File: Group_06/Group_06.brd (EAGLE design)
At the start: 100 x 80 mm, 18 parts, among them J1 POWER_JACKPTH_LOCK, U2 +12v

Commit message: CY8
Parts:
- added D1: BLUE, SparkFun-LED:LED-1206
- added J3: (no value), SparkFun-Connectors:1X06_LOCK
- added R11: (no value), SparkFun-Resistors:AXIAL-0.3
- added U$2: CY8CKIT-059_TARGET_3, CY8KIT-059:CY8CKIT-059_TARGET_3
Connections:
- new net GND2: U$2.52
- new net MUX_A0/2.3C: U$2.24
- new net MUX_A1/2.3C: U$2.23
- new net MUX_A2/2.3C: U$2.22
- new net MUX_OUT/2.5C: U$2.21
- new net N$2: D1.C, R11.P$2
- new net N$3: D1.A, U$2.51
- new net N$4: J3.6, U$2.37
- new net N$5: J3.5, U$2.36
- new net N$6: J3.4, U$2.35
- new net N$7: J3.3, U$2.34
- new net N$8: J3.2, U$2.33
- new net N$9: J3.1, U$2.32
- net 5V: now also U$2.26, U$2.27
- net GND: now also R11.P$1, U$2.25, U$2.28
- net I2C_A0: now also U$2.6
- net I2C_A1: now also U$2.7
- net I2C_A2: now also U$2.8
- net I2C_SCL: now also U$2.16
- net I2C_SDA: now also U$2.15
- net PHOTO_OUT: now also U$2.44
- net TEMP_OUT: now also U$2.43
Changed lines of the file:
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@@
 <layers>
 <layer number="1" name="Top" color="4" fill="1" visible="yes" active="yes"/>
+<layer number="2" name="Route2" color="16" fill="1" visible="no" active="no"/>
+<layer number="3" name="Route3" color="17" fill="1" visible="no" active="no"/>
+<layer number="4" name="Route4" color="18" fill="1" visible="no" active="no"/>
+<layer number="5" name="Route5" color="19" fill="1" visible="no" active="no"/>
+<layer number="6" name="Route6" color="25" fill="1" visible="no" active="no"/>
+<layer number="7" name="Route7" color="26" fill="1" visible="no" active="no"/>
+<layer number="8" name="Route8" color="27" fill="1" visible="no" active="no"/>
+<layer number="9" name="Route9" color="28" fill="1" visible="no" active="no"/>
+<layer number="10" name="Route10" color="29" fill="1" visible="no" active="no"/>
+<layer number="11" name="Route11" color="30" fill="1" visible="no" active="no"/>
+<layer number="12" name="Route12" color="20" fill="1" visible="no" active="no"/>
+<layer number="13" name="Route13" color="21" fill="1" visible="no" active="no"/>
+<layer number="14" name="Route14" color="22" fill="1" visible="no" active="no"/>
+<layer number="15" name="Route15" color="23" fill="1" visible="no" active="no"/>
 <layer number="16" name="Bottom" color="1" fill="1" visible="yes" active="yes"/>
 <layer number="17" name="Pads" color="2" fill="1" visible="yes" active="yes"/>
@@
 <attribute name="VALUE" x="-50.8" y="-46.482" size="0.6096" layer="27" font="vector" ratio="20" align="top-center"/>
 </element>
+<element name="U$2" library="CY8KIT-059" package="CY8CKIT-059_TARGET_3" value="CY8CKIT-059_TARGET_3" x="-16.51" y="-59.69" smashed="yes"/>
+<element name="R11" library="SparkFun-Resistors" package="AXIAL-0.3" value=" " x="-48.26" y="-76.2" smashed="yes">
+<attribute name="NAME" x="-48.26" y="-75.184" size="0.6096" layer="25" font="vector" ratio="20" align="bottom-center"/>
+<attribute name="PROD_ID" value=" " x="-48.26" y="-76.2" size="1.778" layer="27" display="off"/>
+<attribute name="VALUE" x="-48.26" y="-77.216" size="0.6096" layer="27" font="vector" ratio="20" align="top-center"/>
+</element>
+<element name="D1" library="SparkFun-LED" package="LED-1206" value="BLUE" x="-50.8" y="-80.01" smashed="yes">
+<attribute name="NAME" x="-50.8" y="-79.0575" size="0.6096" layer="25" font="vector" ratio="20" align="bottom-center"/>
+<attribute name="PROD_ID" value="DIO-09911" x="-50.8" y="-80.01" size="1.778" layer="27" display="off"/>
+<attribute name="VALUE" x="-50.8" y="-80.9625" size="0.6096" layer="27" font="vector" ratio="20" align="top-center"/>
+</element>
+<element name="J3" library="SparkFun-Connectors" package="1X06_LOCK" value="" x="-50.8" y="-85.09" smashed="yes">
+<attribute name="NAME" x="-52.07" y="-83.693" size="0.6096" layer="25" font="vector" ratio="20"/>
+<attribute name="VALUE" x="-52.07" y="-87.376" size="0.6096" layer="27" font="vector" ratio="20"/>
+</element>
 </elements>
 <signals>
@@
 <contactref element="U$1" pad="3"/>
 <contactref element="U$1" pad="8"/>
+<contactref element="R11" pad="P$1"/>
+<contactref element="U$2" pad="28"/>
+<contactref element="U$2" pad="25"/>
+<wire x1="-46.99" y1="-50.8" x2="-52.07" y2="-76.2" width="0" layer="19" extent="1-1"/>
+<wire x1="-43.18" y1="-15.24" x2="-46.99" y2="-50.8" width="0" layer="19" extent="1-1"/>
+<wire x1="-52.43" y1="-13.705" x2="-43.18" y2="-15.24" width="0" layer="19" extent="1-1"/>
 <wire x1="-52.43" y1="-10.455" x2="-52.43" y2="-13.705" width="0" layer="19" extent="1-1"/>
-<wire x1="-43.18" y1="-15.24" x2="-52.43" y2="-13.705" width="0" layer="19" extent="1-1"/>
 <wire x1="-33.02" y1="-3.85" x2="-43.18" y2="-15.24" width="0" layer="19" extent="1-1"/>
 <wire x1="-24.5" y1="-7.62" x2="-33.02" y2="-3.85" width="0" layer="19" extent="1-1"/>
@@
 <wire x1="-12.28" y1="-2.54" x2="-19.0984" y2="6.89" width="0" layer="19" extent="1-1"/>
 <wire x1="-2.54" y1="3.81" x2="-12.28" y2="-2.54" width="0" layer="19" extent="1-1"/>
+<wire x1="11.43" y1="-71.12" x2="-46.99" y2="-50.8" width="0" layer="19" extent="1-1"/>
 </signal>
 <signal name="TEMP_OUT">
 <contactref element="U1" pad="2"/>
+<contactref element="U$2" pad="43"/>
+<wire x1="-3.81" y1="5.715" x2="-26.67" y2="-71.12" width="0" layer="19" extent="1-1"/>
 </signal>
 <signal name="5V">
@@
 <contactref element="R8" pad="2"/>
 <contactref element="R9" pad="2"/>
+<contactref element="U$2" pad="27"/>
+<contactref element="U$2" pad="26"/>
+<wire x1="-49.95" y1="-45.72" x2="-49.53" y2="-50.8" width="0" layer="19" extent="1-1"/>
 <wire x1="-49.95" y1="-41.91" x2="-49.95" y2="-45.72" width="0" layer="19" extent="1-1"/>
 <wire x1="-49.95" y1="-38.1" x2="-49.95" y2="-41.91" width="0" layer="19" extent="1-1"/>
@@
 <wire x1="-8.16" y1="3.81" x2="-25.527" y2="-11.43" width="0" layer="19" extent="1-1"/>
 <wire x1="-5.08" y1="3.81" x2="-8.16" y2="3.81" width="0" layer="19" extent="1-1"/>
+<wire x1="13.97" y1="-71.12" x2="-49.53" y2="-50.8" width="0" layer="19" extent="1-1"/>
 </signal>
 <signal name="PHOTO_OUT">
 <contactref element="R2" pad="2"/>
 <contactref element="R1" pad="1"/>
+<contactref element="U$2" pad="44"/>
+<wire x1="-10.58" y1="-2.54" x2="-29.21" y2="-71.12" width="0" layer="19" extent="1-1"/>
 <wire x1="-12.16" y1="3.81" x2="-10.58" y2="-2.54" width="0" layer="19" extent="1-1"/>
 </signal>
@@
 <signal name="I2C_SDA">
 <contactref element="U$1" pad="15"/>
+<contactref element="U$2" pad="15"/>
+<wire x1="-46.63" y1="-9.805" x2="-21.59" y2="-50.8" width="0" layer="19" extent="1-1"/>
 </signal>
 <signal name="I2C_SCL">
 <contactref element="U$1" pad="14"/>
+<contactref element="U$2" pad="16"/>
+<wire x1="-46.63" y1="-10.455" x2="-24.13" y2="-50.8" width="0" layer="19" extent="1-1"/>
 </signal>
 <signal name="I2C_A0">
 <contactref element="U$1" pad="1"/>
+<contactref element="U$2" pad="6"/>
+<wire x1="1.27" y1="-50.8" x2="-52.43" y2="-9.155" width="0" layer="19" extent="1-1"/>
 </signal>
 <signal name="I2C_A1">
 <contactref element="U$1" pad="2"/>
+<contactref element="U$2" pad="7"/>
+<wire x1="-1.27" y1="-50.8" x2="-52.43" y2="-9.805" width="0" layer="19" extent="1-1"/>
 </signal>
 <signal name="I2C_A2">
 <contactref element="U$1" pad="13"/>
+<contactref element="U$2" pad="8"/>
+<wire x1="-3.81" y1="-50.8" x2="-46.63" y2="-11.105" width="0" layer="19" extent="1-1"/>
+</signal>
+<signal name="GND2">
+<contactref element="U$2" pad="52"/>
+</signal>
+<signal name="N$2">
+<contactref element="R11" pad="P$2"/>
+<contactref element="D1" pad="C"/>
+<wire x1="-44.45" y1="-76.2" x2="-49.3" y2="-80.01" width="0" layer="19" extent="1-1"/>
+</signal>
+<signal name="N$3">
+<contactref element="D1" pad="A"/>
+<contactref element="U$2" pad="51"/>
+<wire x1="-46.99" y1="-71.12" x2="-52.3" y2="-80.01" width="0" layer="19" extent="1-1"/>
+</signal>
+<signal name="N$4">
+<contactref element="J3" pad="6"/>
+<contactref element="U$2" pad="37"/>
+<wire x1="-11.43" y1="-71.12" x2="-38.1" y2="-85.344" width="0" layer="19" extent="1-1"/>
+</signal>
+<signal name="N$5">
+<contactref element="J3" pad="5"/>
+<contactref element="U$2" pad="36"/>
+<wire x1="-8.89" y1="-71.12" x2="-40.64" y2="-85.09" width="0" layer="19" extent="1-1"/>
+</signal>
+<signal name="N$6">
+<contactref element="J3" pad="4"/>
+<contactref element="U$2" pad="35"/>
+<wire x1="-6.35" y1="-71.12" x2="-43.18" y2="-85.344" width="0" layer="19" extent="1-1"/>
+</signal>
+<signal name="N$7">
+<contactref element="J3" pad="3"/>
+<contactref element="U$2" pad="34"/>
+<wire x1="-3.81" y1="-71.12" x2="-45.72" y2="-85.09" width="0" layer="19" extent="1-1"/>
+</signal>
+<signal name="N$8">
+<contactref element="J3" pad="2"/>
+<contactref element="U$2" pad="33"/>
+<wire x1="-1.27" y1="-71.12" x2="-48.26" y2="-85.344" width="0" layer="19" extent="1-1"/>
+</signal>
+<signal name="N$9">
+<contactref element="J3" pad="1"/>
+<contactref element="U$2" pad="32"/>
+<wire x1="1.27" y1="-71.12" x2="-50.8" y2="-85.09" width="0" layer="19" extent="1-1"/>
+</signal>
+<signal name="MUX_A0/2.3C">
+<contactref element="U$2" pad="24"/>
+</signal>
+<signal name="MUX_A1/2.3C">
+<contactref element="U$2" pad="23"/>
+</signal>
+<signal name="MUX_A2/2.3C">
+<contactref element="U$2" pad="22"/>
+</signal>
+<signal name="MUX_OUT/2.5C">
+<contactref element="U$2" pad="21"/>
 </signal>
 </signals>

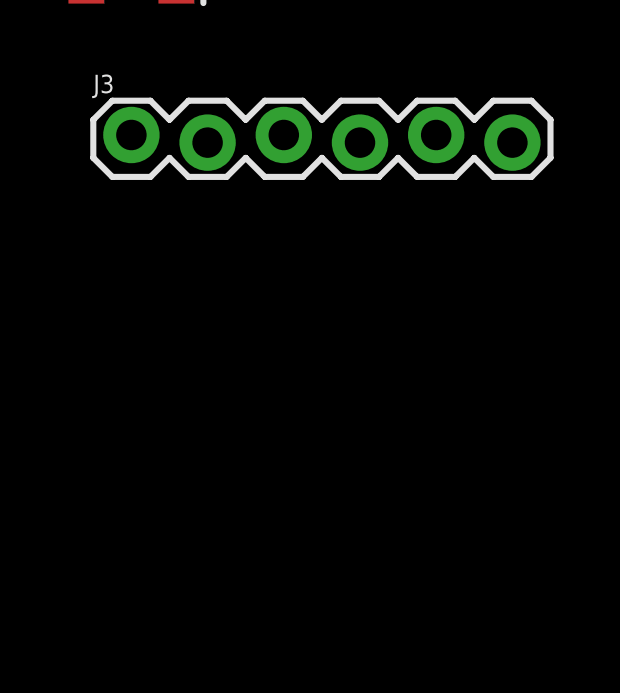
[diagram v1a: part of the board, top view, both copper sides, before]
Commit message: I2C_Connectors and Names
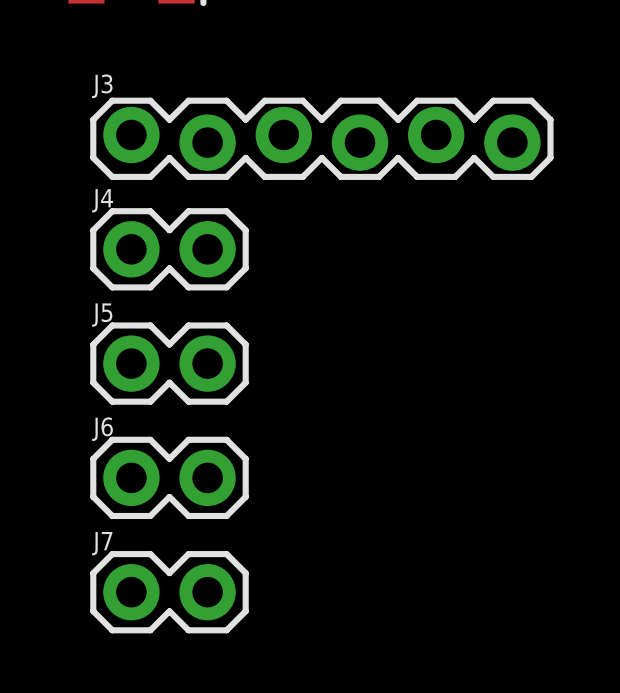
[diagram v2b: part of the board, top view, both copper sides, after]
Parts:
- added J4, J5, J6, J7: (no value), SparkFun-Connectors:1X02
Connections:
- net I2C_SCL_0: now also J4.2
- net I2C_SCL_1: now also J5.2
- net I2C_SCL_2: now also J6.2
- net I2C_SCL_3: now also J7.2
- net I2C_SDA_0: now also J4.1
- net I2C_SDA_1: now also J5.1
- net I2C_SDA_2: now also J6.1
- net I2C_SDA_3: now also J7.1
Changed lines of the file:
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@@
 <attribute name="VALUE" x="-52.07" y="-87.376" size="0.6096" layer="27" font="vector" ratio="20"/>
+</element>
+<element name="J4" library="SparkFun-Connectors" package="1X02" value="" x="-50.8" y="-88.9" smashed="yes">
+<attribute name="NAME" x="-52.07" y="-87.503" size="0.6096" layer="25" font="vector" ratio="20"/>
+<attribute name="VALUE" x="-52.07" y="-90.932" size="0.6096" layer="27" font="vector" ratio="20"/>
+</element>
+<element name="J5" library="SparkFun-Connectors" package="1X02" value="" x="-50.8" y="-92.71" smashed="yes">
+<attribute name="NAME" x="-52.07" y="-91.313" size="0.6096" layer="25" font="vector" ratio="20"/>
+<attribute name="VALUE" x="-52.07" y="-94.742" size="0.6096" layer="27" font="vector" ratio="20"/>
+</element>
+<element name="J6" library="SparkFun-Connectors" package="1X02" value="" x="-50.8" y="-96.52" smashed="yes">
+<attribute name="NAME" x="-52.07" y="-95.123" size="0.6096" layer="25" font="vector" ratio="20"/>
+<attribute name="VALUE" x="-52.07" y="-98.552" size="0.6096" layer="27" font="vector" ratio="20"/>
+</element>
+<element name="J7" library="SparkFun-Connectors" package="1X02" value="" x="-50.8" y="-100.33" smashed="yes">
+<attribute name="NAME" x="-52.07" y="-98.933" size="0.6096" layer="25" font="vector" ratio="20"/>
+<attribute name="VALUE" x="-52.07" y="-102.362" size="0.6096" layer="27" font="vector" ratio="20"/>
 </element>
 </elements>
@@
 <contactref element="U$1" pad="5"/>
 <contactref element="R3" pad="1"/>
+<contactref element="J4" pad="2"/>
+<wire x1="-51.65" y1="-19.05" x2="-48.26" y2="-88.9" width="0" layer="19" extent="1-1"/>
 <wire x1="-52.43" y1="-11.755" x2="-51.65" y2="-19.05" width="0" layer="19" extent="1-1"/>
 </signal>
@@
 <contactref element="U$1" pad="4"/>
 <contactref element="R4" pad="1"/>
+<contactref element="J4" pad="1"/>
+<wire x1="-51.65" y1="-22.86" x2="-50.8" y2="-88.9" width="0" layer="19" extent="1-1"/>
 <wire x1="-52.43" y1="-11.105" x2="-51.65" y2="-22.86" width="0" layer="19" extent="1-1"/>
 </signal>
@@
 <contactref element="U$1" pad="7"/>
 <contactref element="R5" pad="1"/>
+<contactref element="J5" pad="2"/>
+<wire x1="-51.65" y1="-26.67" x2="-48.26" y2="-92.71" width="0" layer="19" extent="1-1"/>
 <wire x1="-52.43" y1="-13.055" x2="-51.65" y2="-26.67" width="0" layer="19" extent="1-1"/>
 </signal>
@@
 <contactref element="U$1" pad="6"/>
 <contactref element="R6" pad="1"/>
+<contactref element="J5" pad="1"/>
+<wire x1="-51.65" y1="-30.48" x2="-50.8" y2="-92.71" width="0" layer="19" extent="1-1"/>
 <wire x1="-52.43" y1="-12.405" x2="-51.65" y2="-30.48" width="0" layer="19" extent="1-1"/>
 </signal>
@@
 <contactref element="U$1" pad="10"/>
 <contactref element="R7" pad="1"/>
+<contactref element="J6" pad="2"/>
+<wire x1="-51.65" y1="-34.29" x2="-48.26" y2="-96.52" width="0" layer="19" extent="1-1"/>
 <wire x1="-46.63" y1="-13.055" x2="-51.65" y2="-34.29" width="0" layer="19" extent="1-1"/>
 </signal>
@@
 <contactref element="U$1" pad="9"/>
 <contactref element="R8" pad="1"/>
+<contactref element="J6" pad="1"/>
+<wire x1="-51.65" y1="-38.1" x2="-50.8" y2="-96.52" width="0" layer="19" extent="1-1"/>
 <wire x1="-46.63" y1="-13.705" x2="-51.65" y2="-38.1" width="0" layer="19" extent="1-1"/>
 </signal>
@@
 <contactref element="U$1" pad="12"/>
 <contactref element="R9" pad="1"/>
+<contactref element="J7" pad="2"/>
+<wire x1="-51.65" y1="-41.91" x2="-48.26" y2="-100.33" width="0" layer="19" extent="1-1"/>
 <wire x1="-46.63" y1="-11.755" x2="-51.65" y2="-41.91" width="0" layer="19" extent="1-1"/>
 </signal>
@@
 <contactref element="U$1" pad="11"/>
 <contactref element="R10" pad="1"/>
+<contactref element="J7" pad="1"/>
+<wire x1="-51.65" y1="-45.72" x2="-50.8" y2="-100.33" width="0" layer="19" extent="1-1"/>
 <wire x1="-46.63" y1="-12.405" x2="-51.65" y2="-45.72" width="0" layer="19" extent="1-1"/>
 </signal>

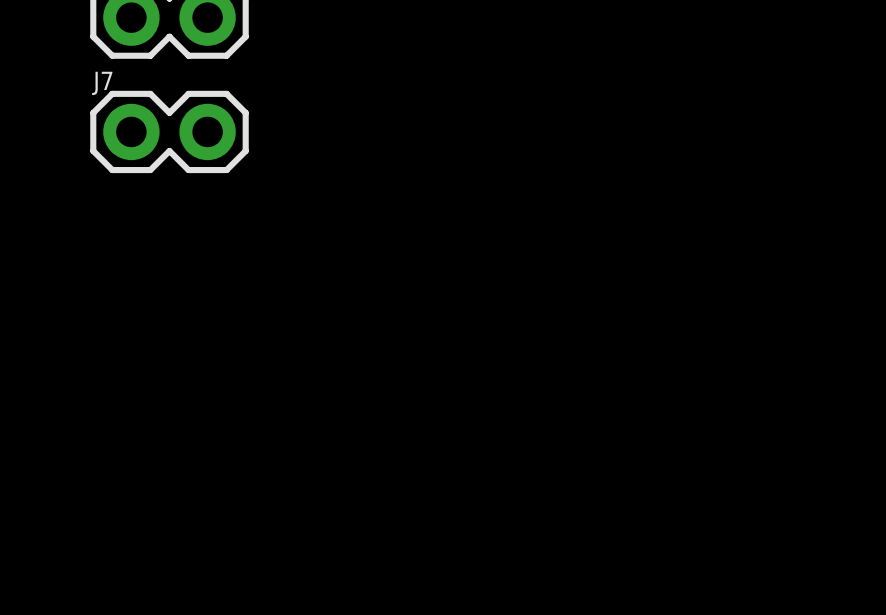
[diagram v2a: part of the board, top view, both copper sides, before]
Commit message: Adding TMUX1208
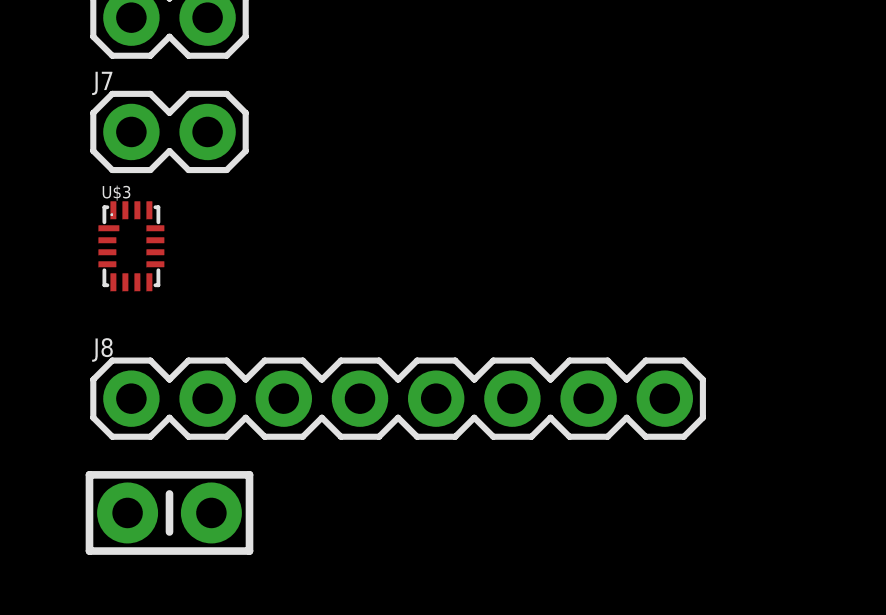
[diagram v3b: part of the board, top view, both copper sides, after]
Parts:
- added C3: 0.1uF, SparkFun-Capacitors:CAP-PTH-SMALL-KIT
- added J8: (no value), SparkFun-Connectors:1X08
- added U$3: TMUX1208RSV, Group_06_Library:QFN-16
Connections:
- new net MUX_A0/1.3C: U$3.15
- new net N$10: J8.8, U$3.2
- new net N$11: J8.7, U$3.3
- new net N$12: J8.6, U$3.4
- new net N$13: J8.5, U$3.5
- new net N$14: J8.4, U$3.10
- new net N$15: J8.3, U$3.9
- new net N$16: J8.2, U$3.8
- new net N$17: J8.1, U$3.7
- new net N$19: U$3.14
- new net N$20: U$3.13
- new net N$23: U$3.6
- net 5V: now also C3.1, U$3.11, U$3.16
- net GND: now also C3.2, U$3.12
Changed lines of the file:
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@@
 <attribute name="VALUE" x="-52.07" y="-102.362" size="0.6096" layer="27" font="vector" ratio="20"/>
+</element>
+<element name="U$3" library="Group_06_Library" package="QFN-16" value="TMUX1208RSV" x="-50.8" y="-104.14" smashed="yes">
+<attribute name="NAME" x="-51.8" y="-102.54" size="0.4064" layer="25"/>
+<attribute name="VALUE" x="-51.85" y="-106.14" size="0.4064" layer="27"/>
+</element>
+<element name="J8" library="SparkFun-Connectors" package="1X08" value="" x="-50.8" y="-109.22" smashed="yes">
+<attribute name="NAME" x="-52.07" y="-107.823" size="0.6096" layer="25" font="vector" ratio="20"/>
+<attribute name="PROD_ID" value="CONN-08438" x="-54.61" y="-104.14" size="1.778" layer="27" display="off"/>
+<attribute name="VALUE" x="-52.07" y="-111.252" size="0.6096" layer="27" font="vector" ratio="20"/>
+</element>
+<element name="C3" library="SparkFun-Capacitors" package="CAP-PTH-SMALL-KIT" value="0.1uF" x="-49.53" y="-113.03" smashed="yes">
+<attribute name="PROD_ID" value="CAP-08370" x="-54.61" y="-107.95" size="1.778" layer="27" display="off"/>
 </element>
 </elements>
@@
 <contactref element="U$2" pad="28"/>
 <contactref element="U$2" pad="25"/>
+<contactref element="U$3" pad="12"/>
+<contactref element="C3" pad="2"/>
+<wire x1="-50" y1="-103.54" x2="-48.133" y2="-113.03" width="0" layer="19" extent="1-1"/>
+<wire x1="-52.07" y1="-76.2" x2="-50" y2="-103.54" width="0" layer="19" extent="1-1"/>
 <wire x1="-46.99" y1="-50.8" x2="-52.07" y2="-76.2" width="0" layer="19" extent="1-1"/>
 <wire x1="-43.18" y1="-15.24" x2="-46.99" y2="-50.8" width="0" layer="19" extent="1-1"/>
@@
 <contactref element="U$2" pad="27"/>
 <contactref element="U$2" pad="26"/>
+<contactref element="U$3" pad="16"/>
+<contactref element="C3" pad="1"/>
+<contactref element="U$3" pad="11"/>
+<wire x1="-50" y1="-103.94" x2="-50.927" y2="-113.03" width="0" layer="19" extent="1-1"/>
+<wire x1="-51.4" y1="-102.94" x2="-50" y2="-103.94" width="0" layer="19" extent="1-1"/>
+<wire x1="-49.53" y1="-50.8" x2="-51.4" y2="-102.94" width="0" layer="19" extent="1-1"/>
 <wire x1="-49.95" y1="-45.72" x2="-49.53" y2="-50.8" width="0" layer="19" extent="1-1"/>
 <wire x1="-49.95" y1="-41.91" x2="-49.95" y2="-45.72" width="0" layer="19" extent="1-1"/>
@@
 <contactref element="U$2" pad="21"/>
 </signal>
+<signal name="N$10">
+<contactref element="J8" pad="8"/>
+<contactref element="U$3" pad="2"/>
+<wire x1="-33.02" y1="-109.22" x2="-51.6" y2="-103.94" width="0" layer="19" extent="1-1"/>
+</signal>
+<signal name="N$11">
+<contactref element="J8" pad="7"/>
+<contactref element="U$3" pad="3"/>
+<wire x1="-35.56" y1="-109.22" x2="-51.6" y2="-104.34" width="0" layer="19" extent="1-1"/>
+</signal>
+<signal name="N$12">
+<contactref element="J8" pad="6"/>
+<contactref element="U$3" pad="4"/>
+<wire x1="-38.1" y1="-109.22" x2="-51.6" y2="-104.74" width="0" layer="19" extent="1-1"/>
+</signal>
+<signal name="N$13">
+<contactref element="J8" pad="5"/>
+<contactref element="U$3" pad="5"/>
+<wire x1="-40.64" y1="-109.22" x2="-51.4" y2="-105.34" width="0" layer="19" extent="1-1"/>
+</signal>
+<signal name="N$14">
+<contactref element="J8" pad="4"/>
+<contactref element="U$3" pad="10"/>
+<wire x1="-50" y1="-104.34" x2="-43.18" y2="-109.22" width="0" layer="19" extent="1-1"/>
+</signal>
+<signal name="N$15">
+<contactref element="J8" pad="3"/>
+<contactref element="U$3" pad="9"/>
+<wire x1="-50" y1="-104.74" x2="-45.72" y2="-109.22" width="0" layer="19" extent="1-1"/>
+</signal>
+<signal name="N$16">
+<contactref element="J8" pad="2"/>
+<contactref element="U$3" pad="8"/>
+<wire x1="-50.2" y1="-105.34" x2="-48.26" y2="-109.22" width="0" layer="19" extent="1-1"/>
+</signal>
+<signal name="N$17">
+<contactref element="J8" pad="1"/>
+<contactref element="U$3" pad="7"/>
+<wire x1="-50.6" y1="-105.34" x2="-50.8" y2="-109.22" width="0" layer="19" extent="1-1"/>
+</signal>
+<signal name="MUX_A0/1.3C">
+<contactref element="U$3" pad="15"/>
+</signal>
+<signal name="N$19">
+<contactref element="U$3" pad="14"/>
+</signal>
+<signal name="N$20">
+<contactref element="U$3" pad="13"/>
+</signal>
+<signal name="N$23">
+<contactref element="U$3" pad="6"/>
+</signal>
 </signals>
